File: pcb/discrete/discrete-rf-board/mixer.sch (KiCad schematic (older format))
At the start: 51 parts, among them J7 UFL, J8 UFL, Q1 NSVT65011MW6T1G, Q2 BCM857BS-7-F, Q3 Q_NPN_BCE, Q4 BCM857BS-7-F, Q5 NSVT65011MW6T1G, T1 HHM1515B2, U3 LT5560EDD#PBF

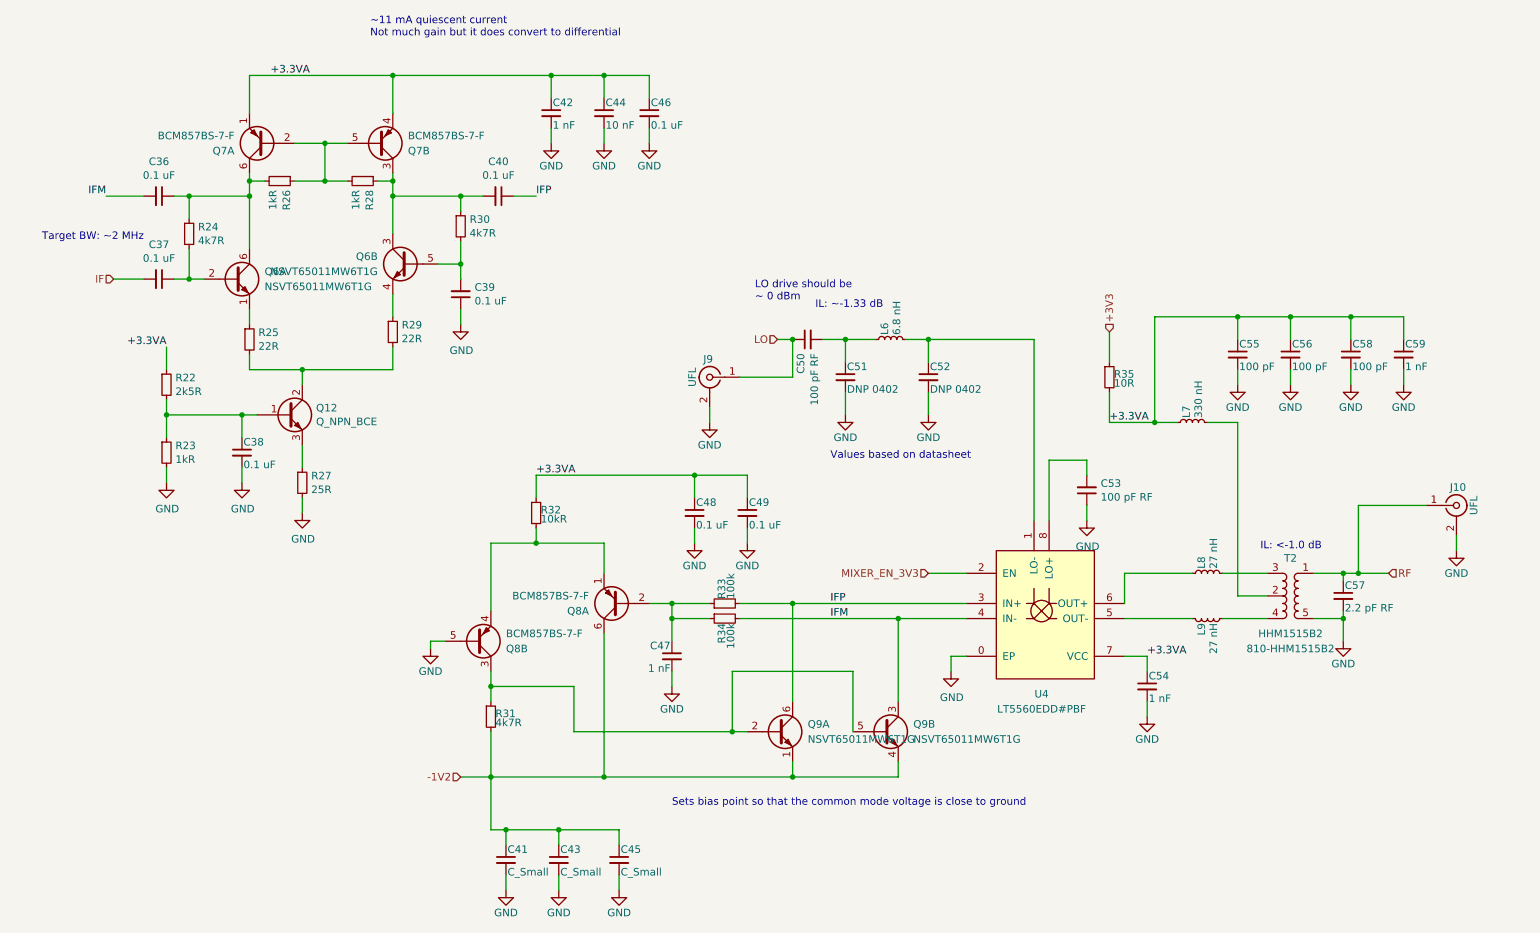
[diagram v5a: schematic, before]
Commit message: All component values set (TODO change transistor gain stages to match values from experimentation
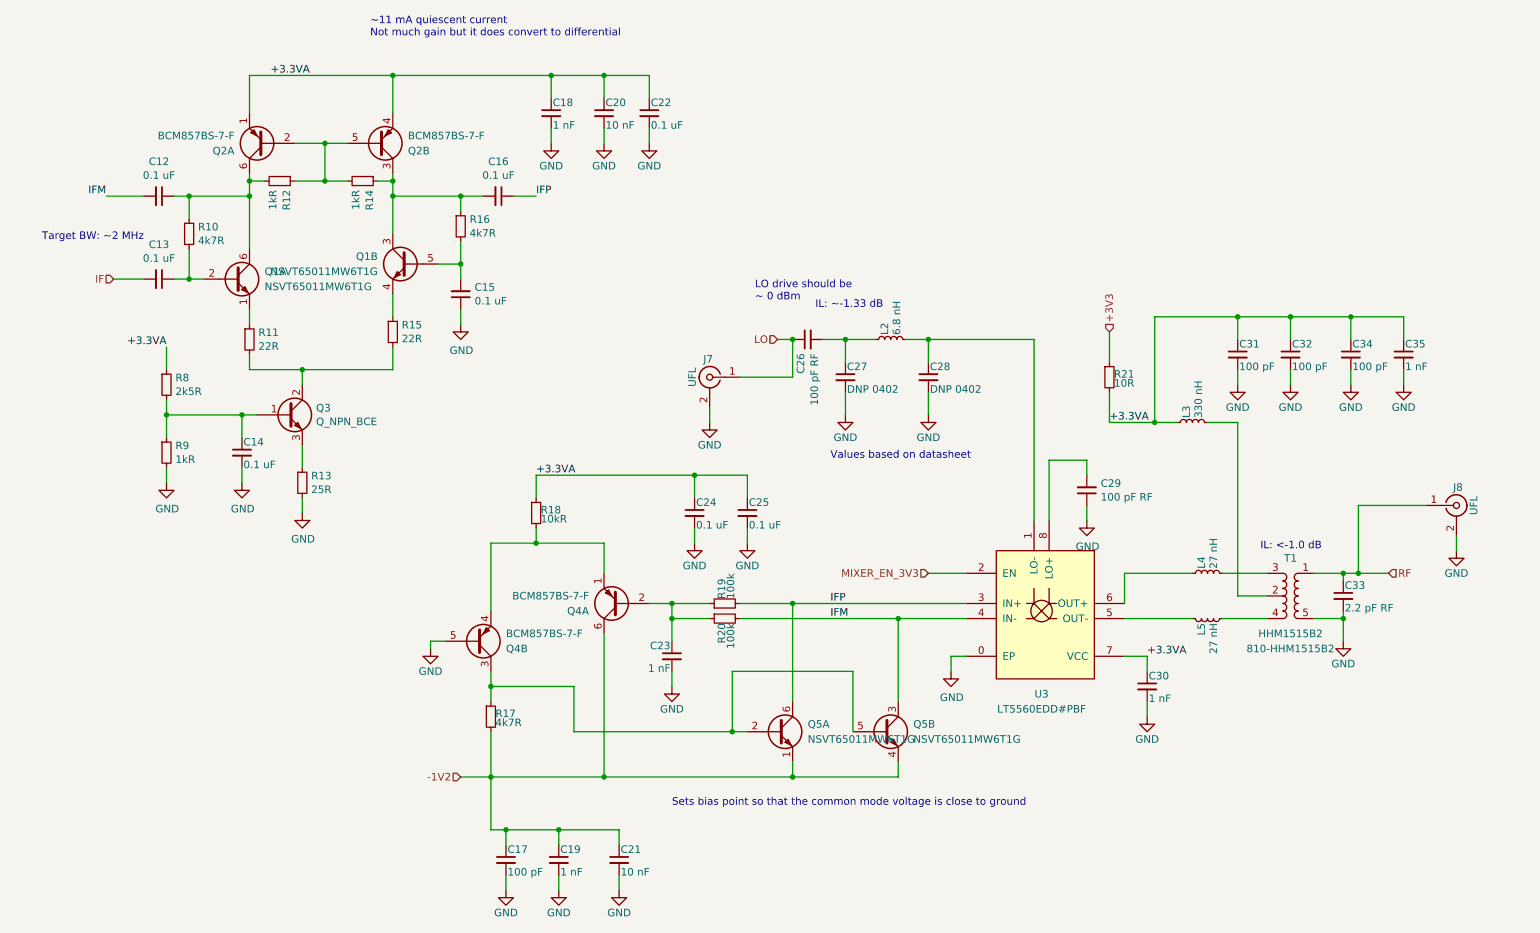
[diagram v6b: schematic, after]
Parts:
- C17: value C_Small -> 100 pF
- C19: value C_Small -> 1 nF
- C21: value C_Small -> 10 nF

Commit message: Autofill; lots left to do
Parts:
- J7, J8: footprint (none) -> discrete_footprints:2337019-1; Mouser (none) -> 571-2337019-1
- Q1, Q5: Mouser (none) -> 863-NSVT65011MW6T1G
- Q2, Q4: Mouser (none) -> 621-BCM857BS-7-F
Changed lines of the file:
@@
 AR Path="/5CA6B0B3/5CC199E0/5D0F4BFE" Ref="#PWR048"  Part="1"
 AR Path="/5CA6B0B3/5CC199E2/5D0F4BFE" Ref="#PWR074"  Part="1"
-F 0 "#PWR048" H 7350 3900 50  0001 C CNN
+F 0 "#PWR074" H 7350 3900 50  0001 C CNN
 F 1 "GND" H 7355 3977 50  0000 C CNN
 F 2 "" H 7350 4150 50  0001 C CNN
@@
 AR Path="/5CA6B0B3/5CC199E0/5D101EA1" Ref="#PWR045"  Part="1"
 AR Path="/5CA6B0B3/5CC199E2/5D101EA1" Ref="#PWR071"  Part="1"
-F 0 "#PWR045" H 5750 3200 50  0001 C CNN
+F 0 "#PWR071" H 5750 3200 50  0001 C CNN
 F 1 "GND" H 5750 3300 50  0000 C CNN
 F 2 "" H 5750 3450 50  0001 C CNN
@@
 AR Path="/5CA6B0B3/5CC199E0/5D1020F7" Ref="#PWR046"  Part="1"
 AR Path="/5CA6B0B3/5CC199E2/5D1020F7" Ref="#PWR072"  Part="1"
-F 0 "#PWR046" H 6300 3200 50  0001 C CNN
+F 0 "#PWR072" H 6300 3200 50  0001 C CNN
 F 1 "GND" H 6300 3300 50  0000 C CNN
 F 2 "" H 6300 3450 50  0001 C CNN
@@
 F 0 "J8" H 9810 4170 50  0000 C CNN
 F 1 "UFL" V 9915 4050 50  0000 C CNN
-F 2 "" H 9800 4050 50  0001 C CNN
+F 2 "discrete_footprints:2337019-1" H 9800 4050 50  0001 C CNN
 F 3 " ~" H 9800 4050 50  0001 C CNN
+F 4 " 571-2337019-1" H 9800 4050 50  0001 C CNN "Mouser"
 	1    9800 4050
 	1    0    0    -1
@@
 AR Path="/5CA6B0B3/5CC199E0/5CC49A0F" Ref="#PWR055"  Part="1"
 AR Path="/5CA6B0B3/5CC199E2/5CC49A0F" Ref="#PWR081"  Part="1"
-F 0 "#PWR055" H 9800 4100 50  0001 C CNN
+F 0 "#PWR081" H 9800 4100 50  0001 C CNN
 F 1 "GND" H 9800 4200 50  0000 C CNN
 F 2 "" H 9800 4350 50  0001 C CNN
@@
 AR Path="/5CA6B0B3/5CC199E0/5CBC9FE3" Ref="#PWR052"  Part="1"
 AR Path="/5CA6B0B3/5CC199E2/5CBC9FE3" Ref="#PWR078"  Part="1"
-F 0 "#PWR052" H 9050 4700 50  0001 C CNN
+F 0 "#PWR078" H 9050 4700 50  0001 C CNN
 F 1 "GND" H 9050 4800 50  0000 C CNN
 F 2 "" H 9050 4950 50  0001 C CNN
@@
 AR Path="/5CA6B0B3/5CC199E0/5D125BFA" Ref="#PWR049"  Part="1"
 AR Path="/5CA6B0B3/5CC199E2/5D125BFA" Ref="#PWR075"  Part="1"
-F 0 "#PWR049" H 7750 5200 50  0001 C CNN
+F 0 "#PWR075" H 7750 5200 50  0001 C CNN
 F 1 "GND" H 7750 5300 50  0000 C CNN
 F 2 "" H 7750 5450 50  0001 C CNN
@@
 AR Path="/5CA6B0B3/5CC199E0/5D0D0BEF" Ref="#PWR047"  Part="1"
 AR Path="/5CA6B0B3/5CC199E2/5D0D0BEF" Ref="#PWR073"  Part="1"
-F 0 "#PWR047" H 6450 4900 50  0001 C CNN
+F 0 "#PWR073" H 6450 4900 50  0001 C CNN
 F 1 "GND" H 6455 4977 50  0000 C CNN
 F 2 "" H 6450 5150 50  0001 C CNN
@@
 AR Path="/5CA6B0B3/5CC199E0/5CB6E137" Ref="#PWR054"  Part="1"
 AR Path="/5CA6B0B3/5CC199E2/5CB6E137" Ref="#PWR080"  Part="1"
-F 0 "#PWR054" H 9450 3000 50  0001 C CNN
+F 0 "#PWR080" H 9450 3000 50  0001 C CNN
 F 1 "GND" H 9450 3100 50  0000 C CNN
 F 2 "" H 9450 3250 50  0001 C CNN
@@
 AR Path="/5CA6B0B3/5CC199E0/5CB6DF60" Ref="#PWR053"  Part="1"
 AR Path="/5CA6B0B3/5CC199E2/5CB6DF60" Ref="#PWR079"  Part="1"
-F 0 "#PWR053" H 9100 3000 50  0001 C CNN
+F 0 "#PWR079" H 9100 3000 50  0001 C CNN
 F 1 "GND" H 9100 3100 50  0000 C CNN
 F 2 "" H 9100 3250 50  0001 C CNN
@@
 AR Path="/5CA6B0B3/5CC199E0/5CB6DBAF" Ref="#PWR051"  Part="1"
 AR Path="/5CA6B0B3/5CC199E2/5CB6DBAF" Ref="#PWR077"  Part="1"
-F 0 "#PWR051" H 8700 3000 50  0001 C CNN
+F 0 "#PWR077" H 8700 3000 50  0001 C CNN
 F 1 "GND" H 8700 3100 50  0000 C CNN
 F 2 "" H 8700 3250 50  0001 C CNN
@@
 AR Path="/5CA6B0B3/5CC199E0/5CB6D892" Ref="#PWR050"  Part="1"
 AR Path="/5CA6B0B3/5CC199E2/5CB6D892" Ref="#PWR076"  Part="1"
-F 0 "#PWR050" H 8350 3000 50  0001 C CNN
+F 0 "#PWR076" H 8350 3000 50  0001 C CNN
 F 1 "GND" H 8350 3100 50  0000 C CNN
 F 2 "" H 8350 3250 50  0001 C CNN
@@
 AR Path="/5CA6B0B3/5CC199E0/5D193951" Ref="#PWR041"  Part="1"
 AR Path="/5CA6B0B3/5CC199E2/5D193951" Ref="#PWR067"  Part="1"
-F 0 "#PWR041" H 4600 5000 50  0001 C CNN
+F 0 "#PWR067" H 4600 5000 50  0001 C CNN
 F 1 "GND" H 4600 5100 50  0000 C CNN
 F 2 "" H 4600 5250 50  0001 C CNN
@@
 AR Path="/5CA6B0B3/5CC199E0/5D1B2EB0" Ref="#PWR033"  Part="1"
 AR Path="/5CA6B0B3/5CC199E2/5D1B2EB0" Ref="#PWR059"  Part="1"
-F 0 "#PWR033" H 3000 4750 50  0001 C CNN
+F 0 "#PWR059" H 3000 4750 50  0001 C CNN
 F 1 "GND" H 3000 4850 50  0000 C CNN
 F 2 "" H 3000 5000 50  0001 C CNN
@@
 AR Path="/5CA6B0B3/5CC199E0/5D1F5C64" Ref="#PWR039"  Part="1"
 AR Path="/5CA6B0B3/5CC199E2/5D1F5C64" Ref="#PWR065"  Part="1"
-F 0 "#PWR039" H 4250 6350 50  0001 C CNN
+F 0 "#PWR065" H 4250 6350 50  0001 C CNN
 F 1 "GND" H 4250 6450 50  0000 C CNN
 F 2 "" H 4250 6600 50  0001 C CNN
@@
 AR Path="/5CA6B0B3/5CC199E0/5D1F5F88" Ref="#PWR037"  Part="1"
 AR Path="/5CA6B0B3/5CC199E2/5D1F5F88" Ref="#PWR063"  Part="1"
-F 0 "#PWR037" H 3850 6350 50  0001 C CNN
+F 0 "#PWR063" H 3850 6350 50  0001 C CNN
 F 1 "GND" H 3850 6450 50  0000 C CNN
 F 2 "" H 3850 6600 50  0001 C CNN
@@
 AR Path="/5CA6B0B3/5CC199E0/5D1F629A" Ref="#PWR035"  Part="1"
 AR Path="/5CA6B0B3/5CC199E2/5D1F629A" Ref="#PWR061"  Part="1"
-F 0 "#PWR035" H 3500 6350 50  0001 C CNN
+F 0 "#PWR061" H 3500 6350 50  0001 C CNN
 F 1 "GND" H 3500 6450 50  0000 C CNN
 F 2 "" H 3500 6600 50  0001 C CNN
@@
 AR Path="/5CA6B0B3/5CC199E0/5D1A89A5" Ref="#PWR032"  Part="1"
 AR Path="/5CA6B0B3/5CC199E2/5D1A89A5" Ref="#PWR058"  Part="1"
-F 0 "#PWR032" H 2150 3850 50  0001 C CNN
+F 0 "#PWR058" H 2150 3850 50  0001 C CNN
 F 1 "GND" H 2155 3927 50  0000 C CNN
 F 2 "" H 2150 4100 50  0001 C CNN
@@
 AR Path="/5CA6B0B3/5CC199E0/5D1A9311" Ref="#PWR030"  Part="1"
 AR Path="/5CA6B0B3/5CC199E2/5D1A9311" Ref="#PWR056"  Part="1"
-F 0 "#PWR030" H 1250 3650 50  0001 C CNN
+F 0 "#PWR056" H 1250 3650 50  0001 C CNN
 F 1 "GND" H 1255 3727 50  0000 C CNN
 F 2 "" H 1250 3900 50  0001 C CNN
@@
 AR Path="/5CA6B0B3/5CC199E0/5D1ABF37" Ref="#PWR031"  Part="1"
 AR Path="/5CA6B0B3/5CC199E2/5D1ABF37" Ref="#PWR057"  Part="1"
-F 0 "#PWR031" H 1750 3650 50  0001 C CNN
+F 0 "#PWR057" H 1750 3650 50  0001 C CNN
 F 1 "GND" H 1755 3727 50  0000 C CNN
 F 2 "" H 1750 3900 50  0001 C CNN
@@
 AR Path="/5CA6B0B3/5CC199E0/5D1AE084" Ref="#PWR034"  Part="1"
 AR Path="/5CA6B0B3/5CC199E2/5D1AE084" Ref="#PWR060"  Part="1"
-F 0 "#PWR034" H 3200 2600 50  0001 C CNN
+F 0 "#PWR060" H 3200 2600 50  0001 C CNN
 F 1 "GND" H 3205 2677 50  0000 C CNN
 F 2 "" H 3200 2850 50  0001 C CNN
@@
 F 0 "J7" H 4860 3320 50  0000 C CNN
 F 1 "UFL" V 4965 3200 50  0000 C CNN
-F 2 "" H 4850 3200 50  0001 C CNN
+F 2 "discrete_footprints:2337019-1" H 4850 3200 50  0001 C CNN
 F 3 " ~" H 4850 3200 50  0001 C CNN
+F 4 " 571-2337019-1" H 4850 3200 50  0001 C CNN "Mouser"
 	1    4850 3200
 	-1   0    0    -1
@@
 AR Path="/5CA6B0B3/5CC199E0/5D85A260" Ref="#PWR043"  Part="1"
 AR Path="/5CA6B0B3/5CC199E2/5D85A260" Ref="#PWR069"  Part="1"
-F 0 "#PWR043" H 4850 3250 50  0001 C CNN
+F 0 "#PWR069" H 4850 3250 50  0001 C CNN
 F 1 "GND" H 4850 3350 50  0000 C CNN
 F 2 "" H 4850 3500 50  0001 C CNN
@@
 AR Path="/5CA6B0B3/5CC199E0/5DADE110" Ref="#PWR036"  Part="1"
 AR Path="/5CA6B0B3/5CC199E2/5DADE110" Ref="#PWR062"  Part="1"
-F 0 "#PWR036" H 3800 1400 50  0001 C CNN
+F 0 "#PWR062" H 3800 1400 50  0001 C CNN
 F 1 "GND" H 3800 1500 50  0000 C CNN
 F 2 "" H 3800 1650 50  0001 C CNN
@@
 AR Path="/5CA6B0B3/5CC199E0/5DAE8BF5" Ref="#PWR038"  Part="1"
 AR Path="/5CA6B0B3/5CC199E2/5DAE8BF5" Ref="#PWR064"  Part="1"
-F 0 "#PWR038" H 4150 1400 50  0001 C CNN
+F 0 "#PWR064" H 4150 1400 50  0001 C CNN
 F 1 "GND" H 4150 1500 50  0000 C CNN
 F 2 "" H 4150 1650 50  0001 C CNN
@@
 AR Path="/5CA6B0B3/5CC199E0/5DB0FBEB" Ref="#PWR042"  Part="1"
 AR Path="/5CA6B0B3/5CC199E2/5DB0FBEB" Ref="#PWR068"  Part="1"
-F 0 "#PWR042" H 4750 4050 50  0001 C CNN
+F 0 "#PWR068" H 4750 4050 50  0001 C CNN
 F 1 "GND" H 4750 4150 50  0000 C CNN
 F 2 "" H 4750 4300 50  0001 C CNN
@@
 AR Path="/5CA6B0B3/5CC199E0/5DB0FBFA" Ref="#PWR044"  Part="1"
 AR Path="/5CA6B0B3/5CC199E2/5DB0FBFA" Ref="#PWR070"  Part="1"
-F 0 "#PWR044" H 5100 4050 50  0001 C CNN
+F 0 "#PWR070" H 5100 4050 50  0001 C CNN
 F 1 "GND" H 5100 4150 50  0000 C CNN
 F 2 "" H 5100 4300 50  0001 C CNN
@@
 AR Path="/5CA6B0B3/5CC199E0/5DB1C7E1" Ref="#PWR040"  Part="1"
 AR Path="/5CA6B0B3/5CC199E2/5DB1C7E1" Ref="#PWR066"  Part="1"
-F 0 "#PWR040" H 4450 1400 50  0001 C CNN
+F 0 "#PWR066" H 4450 1400 50  0001 C CNN
 F 1 "GND" H 4450 1500 50  0000 C CNN
 F 2 "" H 4450 1650 50  0001 C CNN
@@
 F 2 "Package_TO_SOT_SMD:SOT-363_SC-70-6_Handsoldering" H 3050 2550 50  0001 C CNN
 F 3 "~" H 2850 2450 50  0001 C CNN
+F 4 " 863-NSVT65011MW6T1G" H 2850 2450 50  0001 C CNN "Mouser"
 	2    2850 2450
 	-1   0    0    -1
@@
 F 2 "Package_TO_SOT_SMD:SOT-363_SC-70-6_Handsoldering" H 6200 5650 50  0001 C CNN
 F 3 "~" H 6000 5550 50  0001 C CNN
+F 4 " 863-NSVT65011MW6T1G" H 6000 5550 50  0001 C CNN "Mouser"
 	2    6000 5550
 	1    0    0    -1
@@
 F 2 "Package_TO_SOT_SMD:SOT-363_SC-70-6_Handsoldering" H 2850 1750 50  0001 C CNN
 F 3 "~" H 2650 1650 50  0001 C CNN
+F 4 " 621-BCM857BS-7-F " H 2650 1650 50  0001 C CNN "Mouser"
 	2    2650 1650
 	1    0    0    1
@@
 F 2 "Package_TO_SOT_SMD:SOT-363_SC-70-6_Handsoldering" H 3500 5050 50  0001 C CNN
 F 3 "~" H 3300 4950 50  0001 C CNN
+F 4 " 621-BCM857BS-7-F " H 3300 4950 50  0001 C CNN "Mouser"
 	2    3300 4950
 	1    0    0    1
